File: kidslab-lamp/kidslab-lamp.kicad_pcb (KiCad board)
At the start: 2 copper layers, 87.7 x 130.4 mm, 55 parts, among them J1 HY-4A, J2 pin_header_1x3, J3 pin_header_1x3, U1 Pico, U2 LSM6DS3TR-C

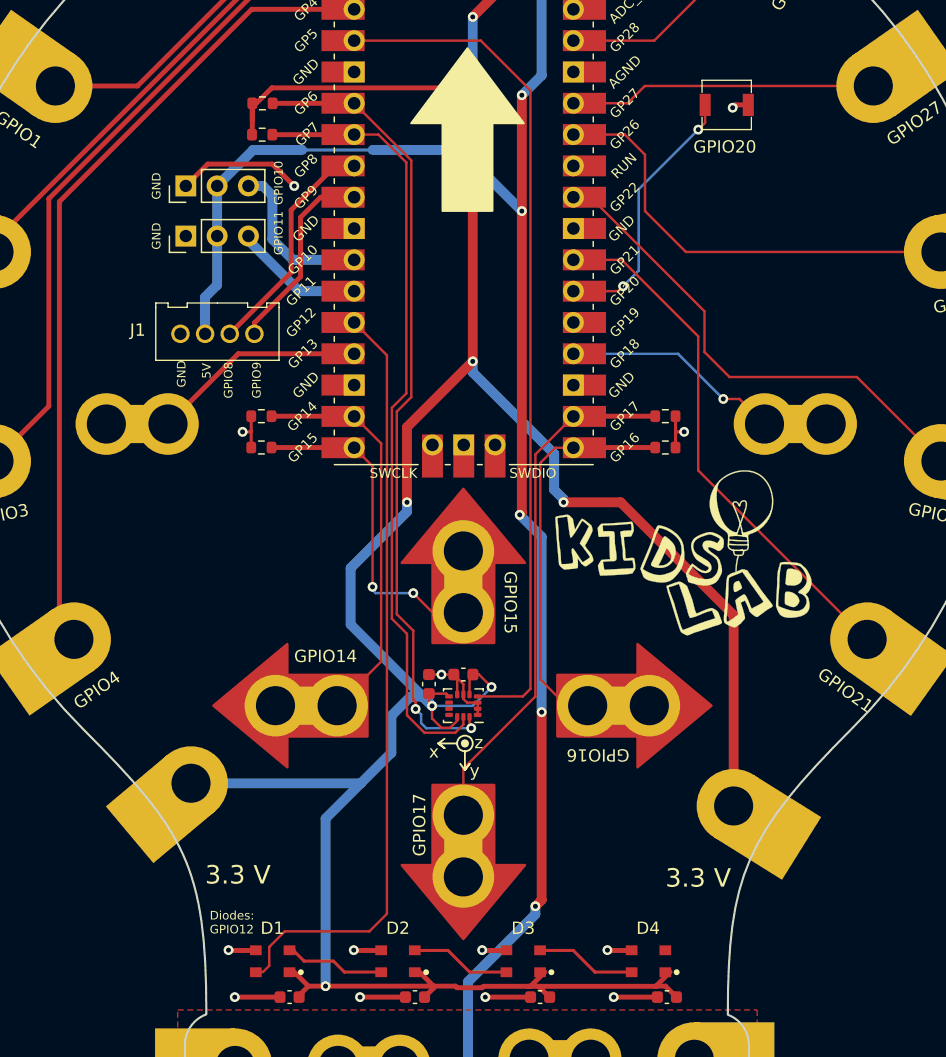
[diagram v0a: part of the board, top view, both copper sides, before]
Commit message: adding polarity information to silkscreen
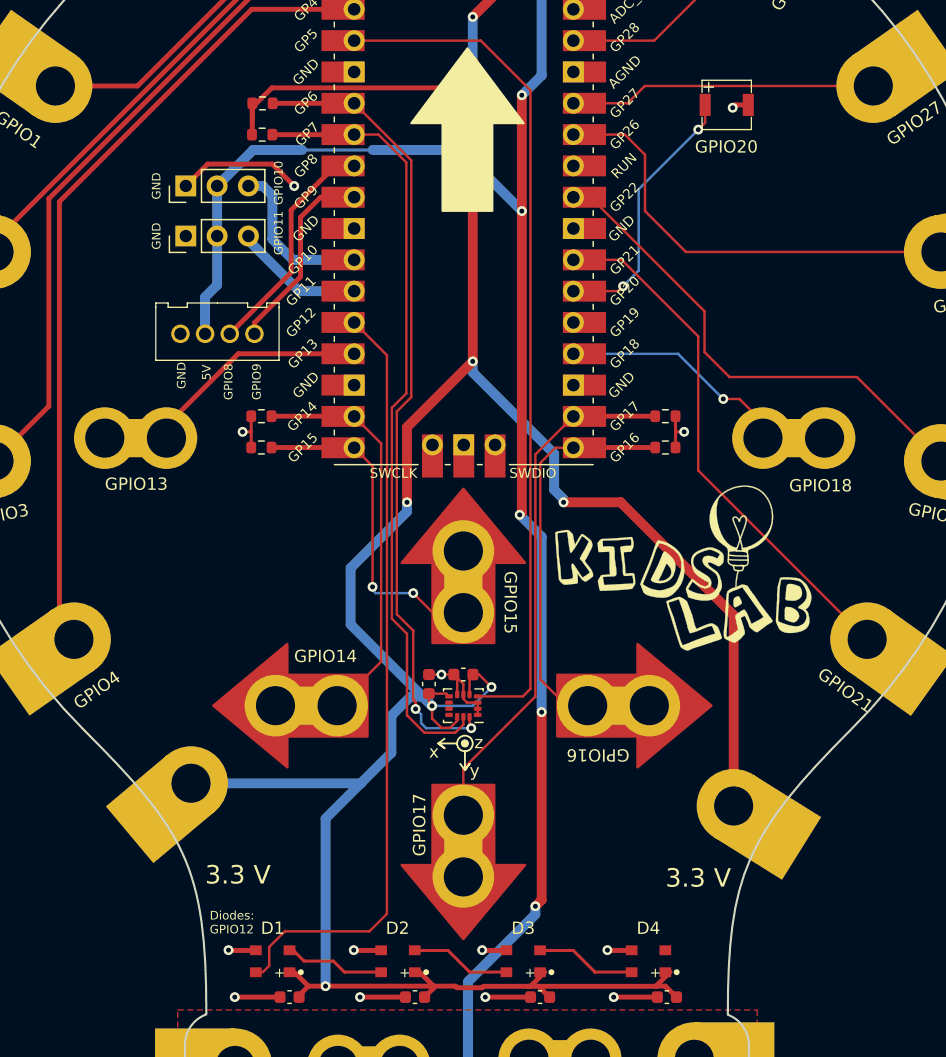
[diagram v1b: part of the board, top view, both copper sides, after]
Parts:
- moved GPIO13 1.15 mm to (123.0, 88.8)
- moved GPIO18 1.15 mm to (176.4, 88.8)
- moved J1 0.50 mm to (129.2, 80.3), turned to 0 degrees
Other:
- board text added: "GPIO13"
- board text added: "GPIO18"
